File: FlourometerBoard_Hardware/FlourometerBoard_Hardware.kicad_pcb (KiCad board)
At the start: 2 copper layers, 105.7 x 36.6 mm, 15 parts, among them J1 RJ45_LED_Shielded, U1 Teensy4.1_DEV-16771, U3 OKI

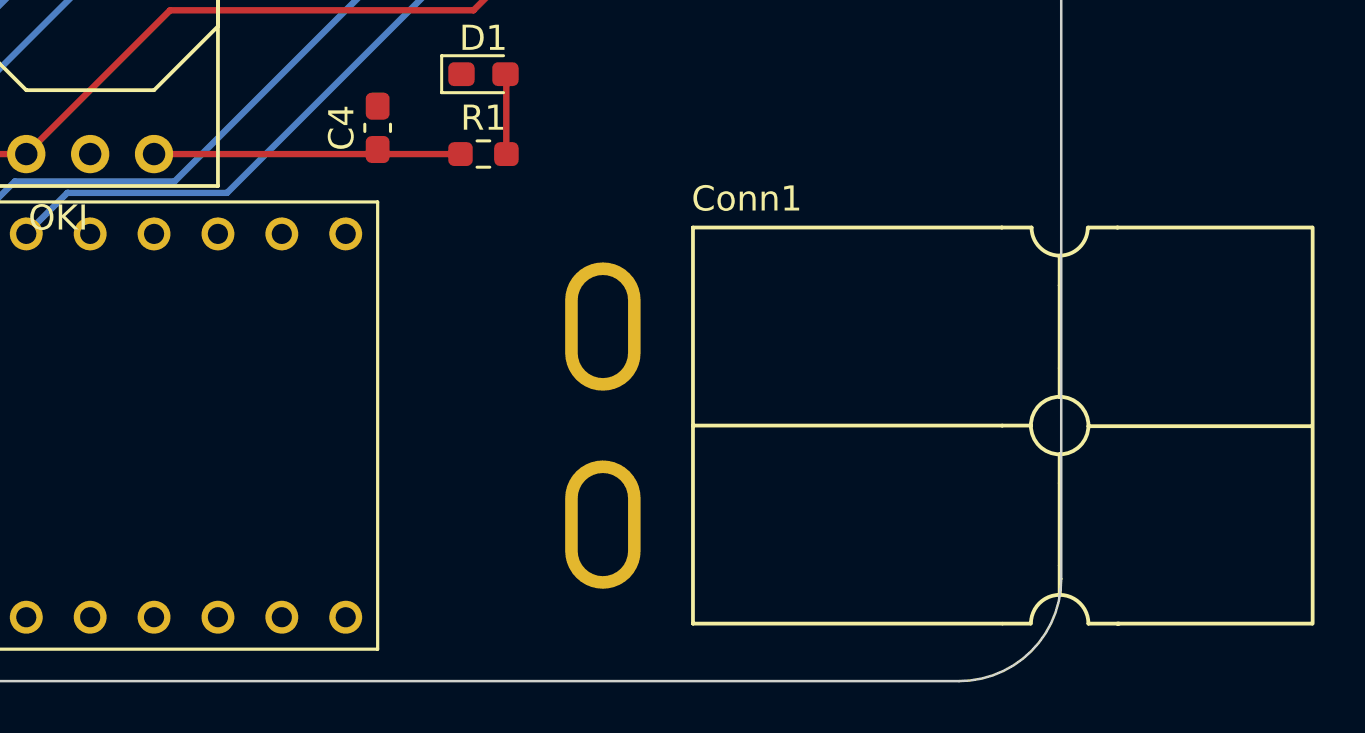
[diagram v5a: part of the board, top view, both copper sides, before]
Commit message: Changed Anderson Footprint from PV
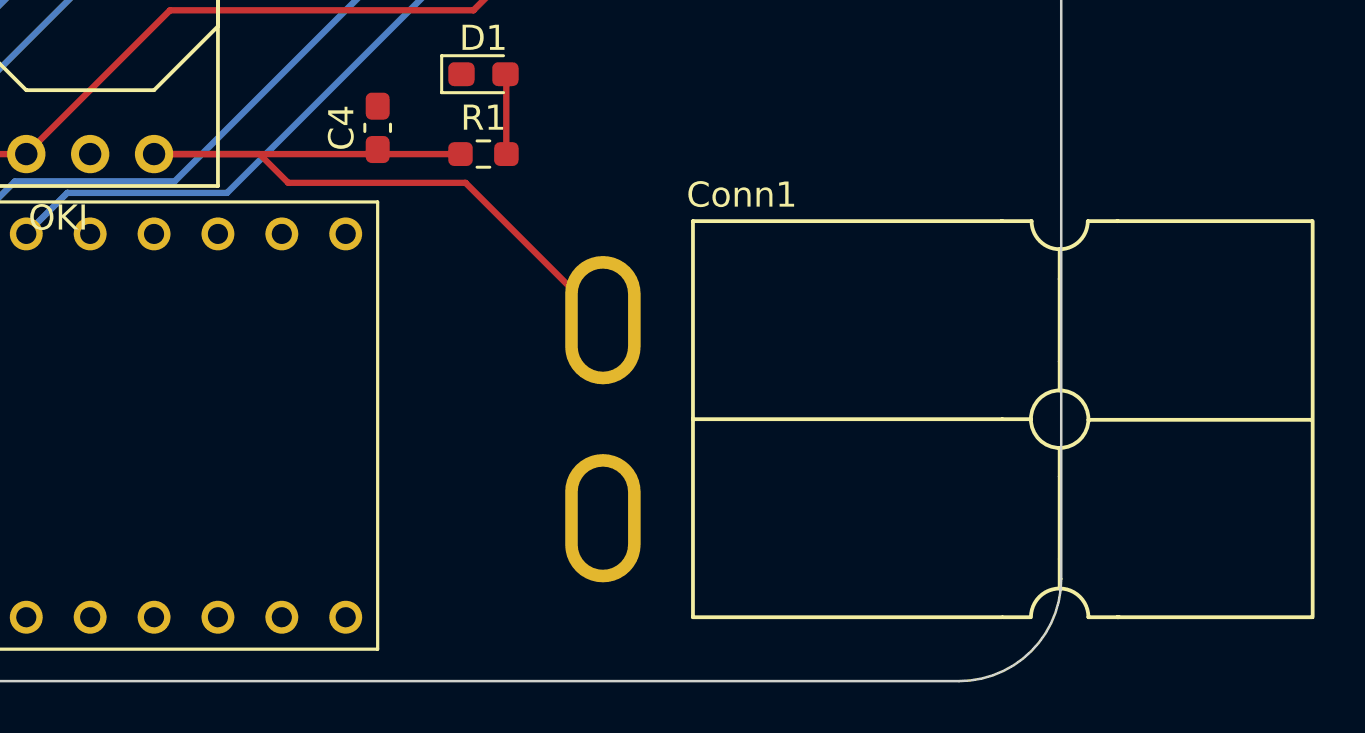
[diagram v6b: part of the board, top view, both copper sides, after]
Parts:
- Conn1: footprint MRDT_Connectors:Square_Anderson_2_H_Side_By_Side_PV -> MRDT_Connectors:Square_Anderson_2_H_Side_By_Side
- moved Conn1 0.25 mm to (125.4, 112.2)
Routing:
- net +12V: track 12.3 -> 32.9 mm
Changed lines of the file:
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@@
       (net 6 "TRG") (pinfunction "A4") (pintype "bidirectional"))
     (pad "19" thru_hole circle (at -11.43 -7.62) (size 1.308 1.308) (drill 0.8) (layers "*.Cu" "*.Mask")
-      (net 54 "unconnected-(U1-A5-Pad19)") (pinfunction "A5") (pintype "bidirectional"))
+      (net 54 "unconnected-(U1-A5-Pad19)") (pinfunction "A5") (pintype "bidirectional+no_connect"))
     (pad "20" thru_hole circle (at -13.97 -7.62) (size 1.308 1.308) (drill 0.8) (layers "*.Cu" "*.Mask")
-      (net 55 "unconnected-(U1-A6-Pad20)") (pinfunction "A6") (pintype "bidirectional"))
+      (net 55 "unconnected-(U1-A6-Pad20)") (pinfunction "A6") (pintype "bidirectional+no_connect"))
     (pad "21" thru_hole circle (at -16.51 -7.62) (size 1.308 1.308) (drill 0.8) (layers "*.Cu" "*.Mask")
-      (net 56 "unconnected-(U1-A7-Pad21)") (pinfunction "A7") (pintype "bidirectional"))
+      (net 56 "unconnected-(U1-A7-Pad21)") (pinfunction "A7") (pintype "bidirectional+no_connect"))
     (pad "22" thru_hole circle (at -19.05 -7.62) (size 1.308 1.308) (drill 0.8) (layers "*.Cu" "*.Mask")
-      (net 57 "unconnected-(U1-A8-Pad22)") (pinfunction "A8") (pintype "bidirectional"))
+      (net 57 "unconnected-(U1-A8-Pad22)") (pinfunction "A8") (pintype "bidirectional+no_connect"))
     (pad "23" thru_hole circle (at -21.59 -7.62) (size 1.308 1.308) (drill 0.8) (layers "*.Cu" "*.Mask")
       (net 39 "unconnected-(U1-A9-Pad23)") (pinfunction "A9") (pintype "bidirectional+no_connect"))
@@
       (clearance 2.5))
   )
-  (footprint "MRDT_Connectors:Square_Anderson_2_H_Side_By_Side_PV" (layer "F.Cu")
-    (at 125.6702 112.187 180)
+  (footprint "MRDT_Connectors:Square_Anderson_2_H_Side_By_Side" (layer "F.Cu")
+    (at 125.4202 112.183 180)
     (property "Sheetfile" "FlourometerBoard_Hardware.kicad_sch")
     (property "Sheetname" "")
     (attr through_hole)
-    (fp_text reference "Conn1" (at -5.85 13.25) (layer "F.SilkS")
-        (effects (font (size 1 1) (thickness 0.15)))
-    )
-    (fp_text value "AndersonPP" (at -17 -4.65) (layer "F.Fab")
-        (effects (font (size 1 1) (thickness 0.15)))
-    )
-    (fp_line (start -28.344 -3.637) (end -28.344 12.111)
-      (stroke (width 0.15) (type solid)) (layer "F.SilkS"))
-    (fp_line (start -28.3186 -3.637) (end -20.5716 -3.637)
-      (stroke (width 0.15) (type solid)) (layer "F.SilkS"))
-    (fp_line (start -28.3186 4.2116) (end -19.4286 4.2116)
-      (stroke (width 0.15) (type solid)) (layer "F.SilkS"))
-    (fp_line (start -20.597 12.111) (end -19.4286 12.111)
-      (stroke (width 0.15) (type solid)) (layer "F.SilkS"))
-    (fp_line (start -20.5716 12.111) (end -28.3186 12.111)
-      (stroke (width 0.15) (type solid)) (layer "F.SilkS"))
-    (fp_line (start -19.4286 -3.637) (end -20.6478 -3.637)
-      (stroke (width 0.15) (type solid)) (layer "F.SilkS"))
-    (fp_line (start -18.2856 -2.494) (end -18.2856 -1.3256)
-      (stroke (width 0.15) (type solid)) (layer "F.SilkS"))
-    (fp_line (start -18.2856 1.951) (end -18.2856 -1.3256)
-      (stroke (width 0.15) (type solid)) (layer "F.SilkS"))
-    (fp_line (start -18.2856 1.951) (end -18.2856 3.094)
-      (stroke (width 0.15) (type solid)) (layer "F.SilkS"))
-    (fp_line (start -18.2856 6.523) (end -18.2856 5.38)
-      (stroke (width 0.15) (type solid)) (layer "F.SilkS"))
-    (fp_line (start -18.2856 6.523) (end -18.2856 9.825)
-      (stroke (width 0.15) (type solid)) (layer "F.SilkS"))
-    (fp_line (start -18.2856 9.7996) (end -18.2856 10.968)
-      (stroke (width 0.15) (type solid)) (layer "F.SilkS"))
-    (fp_line (start -16.025 -3.637) (end -17.1172 -3.637)
-      (stroke (width 0.15) (type solid)) (layer "F.SilkS"))
-    (fp_line (start -15.9996 -3.637) (end -3.706 -3.637)
-      (stroke (width 0.15) (type solid)) (layer "F.SilkS"))
-    (fp_line (start -15.9996 4.237) (end -17.1426 4.237)
-      (stroke (width 0.15) (type solid)) (layer "F.SilkS"))
-    (fp_line (start -15.9996 4.237) (end -3.706 4.237)
-      (stroke (width 0.15) (type solid)) (layer "F.SilkS"))
-    (fp_line (start -15.9996 12.111) (end -3.706 12.111)
-      (stroke (width 0.15) (type solid)) (layer "F.SilkS"))
-    (fp_line (start -15.9742 12.111) (end -17.168 12.111)
-      (stroke (width 0.15) (type solid)) (layer "F.SilkS"))
-    (fp_line (start -3.706 -3.637) (end -3.706 12.111)
-      (stroke (width 0.15) (type solid)) (layer "F.SilkS"))
-    (fp_arc (start -19.4032 12.111) (mid -19.075863 11.320737) (end -18.2856 10.9934)
-      (stroke (width 0.15) (type solid)) (layer "F.SilkS"))
-    (fp_arc (start -18.2856 -2.494) (mid -19.093823 -2.828777) (end -19.4286 -3.637)
-      (stroke (width 0.15) (type solid)) (layer "F.SilkS"))
-    (fp_arc (start -18.2856 10.9934) (mid -17.495337 11.320737) (end -17.168 12.111)
-      (stroke (width 0.15) (type solid)) (layer "F.SilkS"))
-    (fp_arc (start -17.1426 -3.637) (mid -17.477377 -2.828777) (end -18.2856 -2.494)
-      (stroke (width 0.15) (type solid)) (layer "F.SilkS"))
-    (fp_circle (center -18.2856 4.237) (end -18.2856 5.38)
+    (fp_text reference "Conn1" (at -5.9 13.4 180) (layer "F.SilkS")
+        (effects (font (size 1 1) (thickness 0.15)))
+    )
+    (fp_text value "AndersonPP" (at -17.15 -4.7 180) (layer "F.Fab")
+        (effects (font (size 1 1) (thickness 0.15)))
+    )
+    (fp_line (start -28.594 -3.387) (end -28.594 12.361)
+      (stroke (width 0.15) (type solid)) (layer "F.SilkS"))
+    (fp_line (start -28.5686 -3.387) (end -20.8216 -3.387)
+      (stroke (width 0.15) (type solid)) (layer "F.SilkS"))
+    (fp_line (start -28.5686 4.4616) (end -19.6786 4.4616)
+      (stroke (width 0.15) (type solid)) (layer "F.SilkS"))
+    (fp_line (start -20.847 12.361) (end -19.6786 12.361)
+      (stroke (width 0.15) (type solid)) (layer "F.SilkS"))
+    (fp_line (start -20.8216 12.361) (end -28.5686 12.361)
+      (stroke (width 0.15) (type solid)) (layer "F.SilkS"))
+    (fp_line (start -19.6786 -3.387) (end -20.8978 -3.387)
+      (stroke (width 0.15) (type solid)) (layer "F.SilkS"))
+    (fp_line (start -18.5356 -2.244) (end -18.5356 -1.0756)
+      (stroke (width 0.15) (type solid)) (layer "F.SilkS"))
+    (fp_line (start -18.5356 2.201) (end -18.5356 -1.0756)
+      (stroke (width 0.15) (type solid)) (layer "F.SilkS"))
+    (fp_line (start -18.5356 2.201) (end -18.5356 3.344)
+      (stroke (width 0.15) (type solid)) (layer "F.SilkS"))
+    (fp_line (start -18.5356 6.773) (end -18.5356 5.63)
+      (stroke (width 0.15) (type solid)) (layer "F.SilkS"))
+    (fp_line (start -18.5356 6.773) (end -18.5356 10.075)
+      (stroke (width 0.15) (type solid)) (layer "F.SilkS"))
+    (fp_line (start -18.5356 10.0496) (end -18.5356 11.218)
+      (stroke (width 0.15) (type solid)) (layer "F.SilkS"))
+    (fp_line (start -16.275 -3.387) (end -17.3672 -3.387)
+      (stroke (width 0.15) (type solid)) (layer "F.SilkS"))
+    (fp_line (start -16.2496 -3.387) (end -3.956 -3.387)
+      (stroke (width 0.15) (type solid)) (layer "F.SilkS"))
+    (fp_line (start -16.2496 4.487) (end -17.3926 4.487)
+      (stroke (width 0.15) (type solid)) (layer "F.SilkS"))
+    (fp_line (start -16.2496 4.487) (end -3.956 4.487)
+      (stroke (width 0.15) (type solid)) (layer "F.SilkS"))
+    (fp_line (start -16.2496 12.361) (end -3.956 12.361)
+      (stroke (width 0.15) (type solid)) (layer "F.SilkS"))
+    (fp_line (start -16.2242 12.361) (end -17.418 12.361)
+      (stroke (width 0.15) (type solid)) (layer "F.SilkS"))
+    (fp_line (start -3.956 -3.387) (end -3.956 12.361)
+      (stroke (width 0.15) (type solid)) (layer "F.SilkS"))
+    (fp_arc (start -19.6532 12.361) (mid -19.325863 11.570737) (end -18.5356 11.2434)
+      (stroke (width 0.15) (type solid)) (layer "F.SilkS"))
+    (fp_arc (start -18.5356 -2.244) (mid -19.343823 -2.578777) (end -19.6786 -3.387)
+      (stroke (width 0.15) (type solid)) (layer "F.SilkS"))
+    (fp_arc (start -18.5356 11.2434) (mid -17.745337 11.570737) (end -17.418 12.361)
+      (stroke (width 0.15) (type solid)) (layer "F.SilkS"))
+    (fp_arc (start -17.3926 -3.387) (mid -17.727377 -2.578777) (end -18.5356 -2.244)
+      (stroke (width 0.15) (type solid)) (layer "F.SilkS"))
+    (fp_circle (center -18.5356 4.487) (end -18.5356 5.63)
       (stroke (width 0.15) (type solid)) (fill none) (layer "F.SilkS"))
-    (pad "1" thru_hole oval (at -0.1246 0.3 180) (size 3 5.1) (drill oval 2 4.1) (layers "*.Cu" "*.Mask")
+    (pad "1" thru_hole oval (at -0.3746 0.55 180) (size 3 5.1) (drill oval 2 4.1) (layers "*.Cu" "*.Mask" "F.Paste")
       (net 1 "GND") (pinfunction "GND") (pintype "input"))
-    (pad "4" thru_hole oval (at -0.1246 8.174 180) (size 3 5.1) (drill oval 2 4.1) (layers "*.Cu" "*.Mask"))
+    (pad "2" thru_hole oval (at -0.3746 8.424 180) (size 3 5.1) (drill oval 2 4.1) (layers "*.Cu" "*.Mask" "F.Paste")
+      (net 3 "+12V") (pinfunction "V+Log") (pintype "input"))
     (model "C:/Users/Brink/Documents/GitHub/MRDT_KiCAD_Libraries/3D Files/MRDT_Connctors/Anderson_2_Horizontal_Side_by_Side.stp"
       (offset (xyz -3.5 -12 8))
@@
   (segment (start 60.96 88.9) (end 60.96 88.24) (width 0.254) (layer "F.Cu") (net 2))
   (segment (start 117.02 97.155) (end 120.1325 97.155) (width 0.254) (layer "F.Cu") (net 3))
+  (segment (start 113.284 98.298) (end 112.141 97.155) (width 0.25) (layer "F.Cu") (net 3))
   (segment (start 116.84 96.975) (end 117.02 97.155) (width 0.254) (layer "F.Cu") (net 3))
+  (segment (start 120.3338 98.298) (end 113.284 98.298) (width 0.25) (layer "F.Cu") (net 3))
+  (segment (start 112.141 97.155) (end 107.95 97.155) (width 0.25) (layer "F.Cu") (net 3))
+  (segment (start 125.7948 103.759) (end 120.3338 98.298) (width 0.25) (layer "F.Cu") (net 3))
   (segment (start 116.66 97.155) (end 107.95 97.155) (width 0.254) (layer "F.Cu") (net 3))
   (segment (start 116.84 96.975) (end 116.66 97.155) (width 0.254) (layer "F.Cu") (net 3))
